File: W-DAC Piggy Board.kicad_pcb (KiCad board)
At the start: 4 copper layers, 50 x 98.5 mm, 6 parts, among them J1 I2C, J2 W-Output, J3 W-DAC J3, J4 W-DAC J4, J5 W-Output, J6 Power

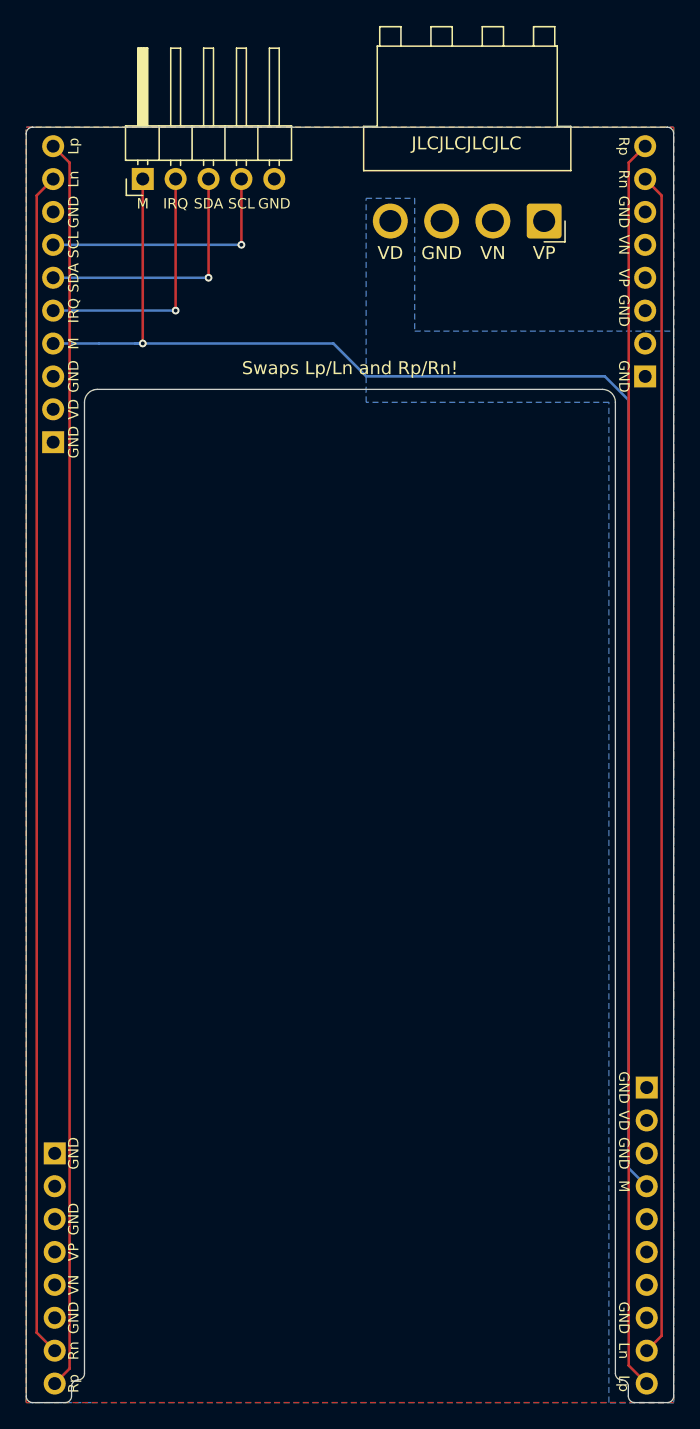
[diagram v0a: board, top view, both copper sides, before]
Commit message: Update to KiCad 6
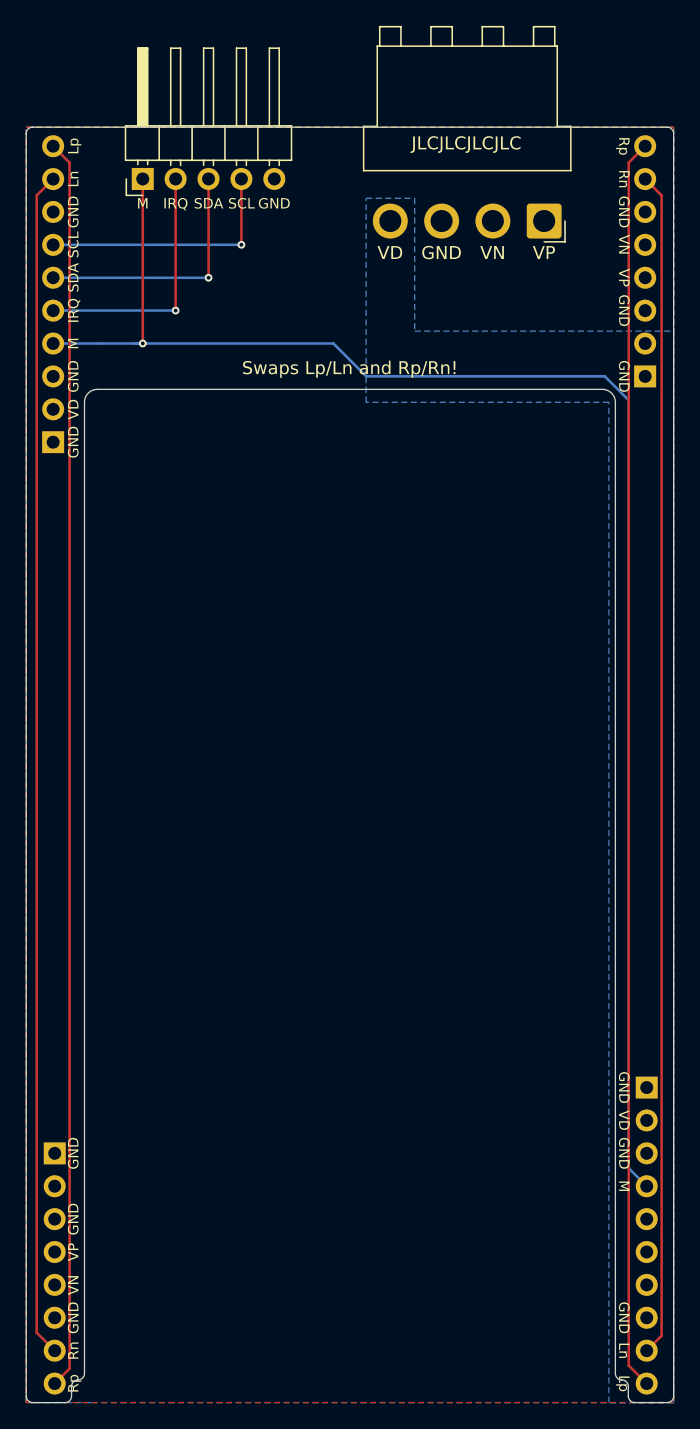
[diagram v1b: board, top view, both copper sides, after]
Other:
- net class Default removed
